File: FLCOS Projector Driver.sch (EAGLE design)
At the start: 61 parts, among them IC2 LM3414, IC3 MIC5219BM5, IC4 MIC5219BM5, IC5 LM3414, IC6 LM3414, Q1 14.31818MHz, Q3 12MHz, T2 S8050, T3 S8050, U1 TVP5150-NTSC_DECODER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

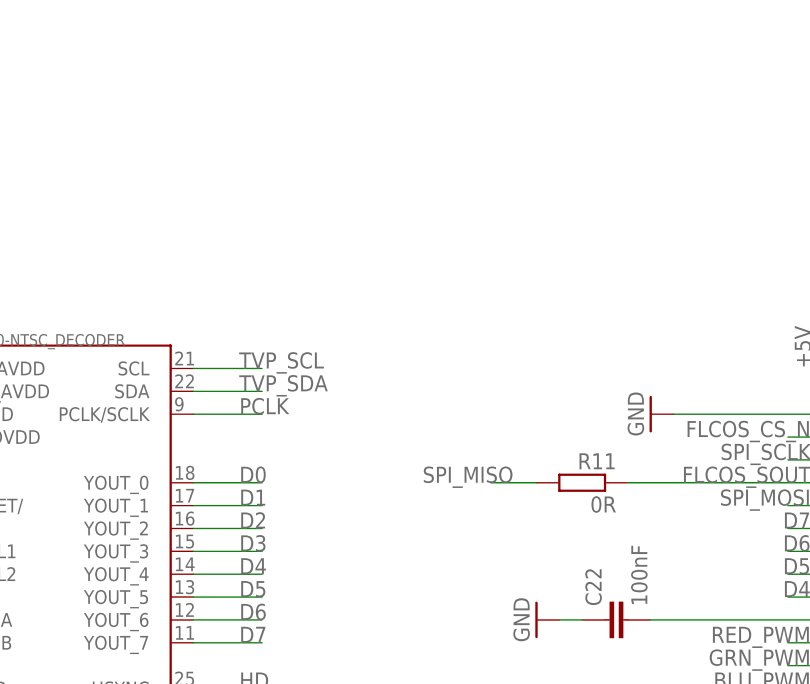
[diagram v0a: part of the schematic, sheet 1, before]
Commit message: added pullups to I2C
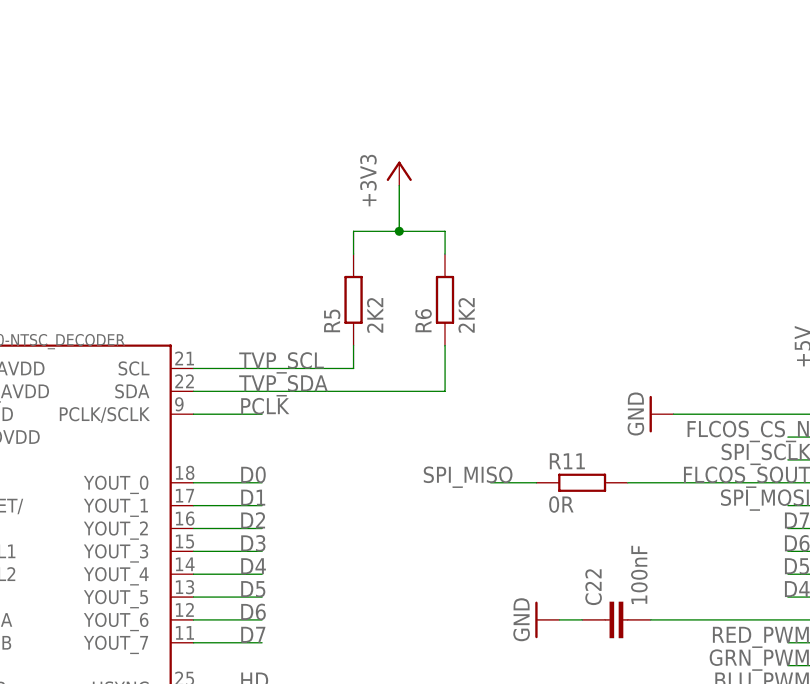
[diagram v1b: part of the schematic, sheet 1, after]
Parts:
- added R5, R6: 2K2, rcl:R-EU_R0603
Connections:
- net +3V3: now also R5.2, R6.2
- net FLCOS_SOUT: now also R11.2; no longer R11.1
- net SPI_MISO: now also R11.1; no longer R11.2
- net TVP_SCL: now also R5.1
- net TVP_SDA: now also R6.1
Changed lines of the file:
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@@
 <part name="P+8" library="supply1" deviceset="+5V" device=""/>
 <part name="P+9" library="supply1" deviceset="+5V" device=""/>
-<part name="R11" library="rcl" deviceset="R-EU_" device="R0603" value="0R"/>
 <part name="IC1" library="SparkFun" deviceset="V_REG_LM1117" device="SOT223"/>
 <part name="RGB" library="con-jst" deviceset="ZH-8" device=""/>
@@
 <part name="P+11" library="supply1" deviceset="+5V" device=""/>
 <part name="P+12" library="supply1" deviceset="+5V" device=""/>
+<part name="+3V3" library="supply1" deviceset="+3V3" device=""/>
+<part name="R11" library="rcl" deviceset="R-EU_" device="R0603" value="0R"/>
+<part name="R5" library="rcl" deviceset="R-EU_" device="R0603" value="2K2"/>
+<part name="R6" library="rcl" deviceset="R-EU_" device="R0603" value="2K2"/>
 </parts>
 <sheets>
@@
 <instance part="IC3" gate="G1" x="-40.64" y="71.12"/>
 <instance part="IC4" gate="G1" x="99.06" y="7.62"/>
-<instance part="R11" gate="G$1" x="109.22" y="63.5" rot="MR0"/>
 <instance part="IC1" gate="G$1" x="-38.1" y="106.68"/>
+<instance part="+3V3" gate="G$1" x="88.9" y="99.06"/>
+<instance part="R11" gate="G$1" x="109.22" y="63.5"/>
+<instance part="R5" gate="G$1" x="83.82" y="83.82" rot="R90"/>
+<instance part="R6" gate="G$1" x="93.98" y="83.82" rot="R90"/>
 </instances>
 <busses>
@@
 <segment>
 <pinref part="U1" gate="G$1" pin="SCL"/>
-<wire x1="66.04" y1="76.2" x2="73.66" y2="76.2" width="0.1524" layer="91"/>
 <label x="71.12" y="76.2" size="1.778" layer="95" rot="MR0" align="bottom-right"/>
+<wire x1="66.04" y1="76.2" x2="83.82" y2="76.2" width="0.1524" layer="91"/>
+<wire x1="83.82" y1="76.2" x2="83.82" y2="78.74" width="0.1524" layer="91"/>
+<pinref part="R5" gate="G$1" pin="1"/>
 </segment>
 </net>
@@
 <segment>
 <pinref part="U1" gate="G$1" pin="SDA"/>
-<wire x1="66.04" y1="73.66" x2="73.66" y2="73.66" width="0.1524" layer="91"/>
 <label x="71.12" y="73.66" size="1.778" layer="95" rot="MR0" align="bottom-right"/>
+<wire x1="66.04" y1="73.66" x2="93.98" y2="73.66" width="0.1524" layer="91"/>
+<wire x1="93.98" y1="73.66" x2="93.98" y2="78.74" width="0.1524" layer="91"/>
+<pinref part="R6" gate="G$1" pin="1"/>
 </segment>
 </net>
@@
 <pinref part="X1" gate="-5" pin="1"/>
 <label x="134.62" y="63.5" size="1.778" layer="95" rot="MR0"/>
-<pinref part="R11" gate="G$1" pin="1"/>
 <wire x1="139.7" y1="63.5" x2="114.3" y2="63.5" width="0.1524" layer="91"/>
+<pinref part="R11" gate="G$1" pin="2"/>
 </segment>
 </net>
@@
 <junction x="33.02" y="68.58"/>
 </segment>
+<segment>
+<wire x1="83.82" y1="88.9" x2="83.82" y2="91.44" width="0.1524" layer="91"/>
+<wire x1="83.82" y1="91.44" x2="88.9" y2="91.44" width="0.1524" layer="91"/>
+<wire x1="88.9" y1="91.44" x2="93.98" y2="91.44" width="0.1524" layer="91"/>
+<wire x1="93.98" y1="91.44" x2="93.98" y2="88.9" width="0.1524" layer="91"/>
+<pinref part="+3V3" gate="G$1" pin="+3V3"/>
+<wire x1="88.9" y1="91.44" x2="88.9" y2="96.52" width="0.1524" layer="91"/>
+<junction x="88.9" y="91.44"/>
+<pinref part="R5" gate="G$1" pin="2"/>
+<pinref part="R6" gate="G$1" pin="2"/>
+</segment>
 </net>
 <net name="EN_N" class="0">
@@
 <net name="SPI_MISO" class="0">
 <segment>
-<pinref part="R11" gate="G$1" pin="2"/>
 <wire x1="104.14" y1="63.5" x2="99.06" y2="63.5" width="0.1524" layer="91"/>
 <label x="101.6" y="63.5" size="1.778" layer="95" rot="MR0"/>
-</segment>
-</net>
+<pinref part="R11" gate="G$1" pin="1"/>
+</segment>
+</net>

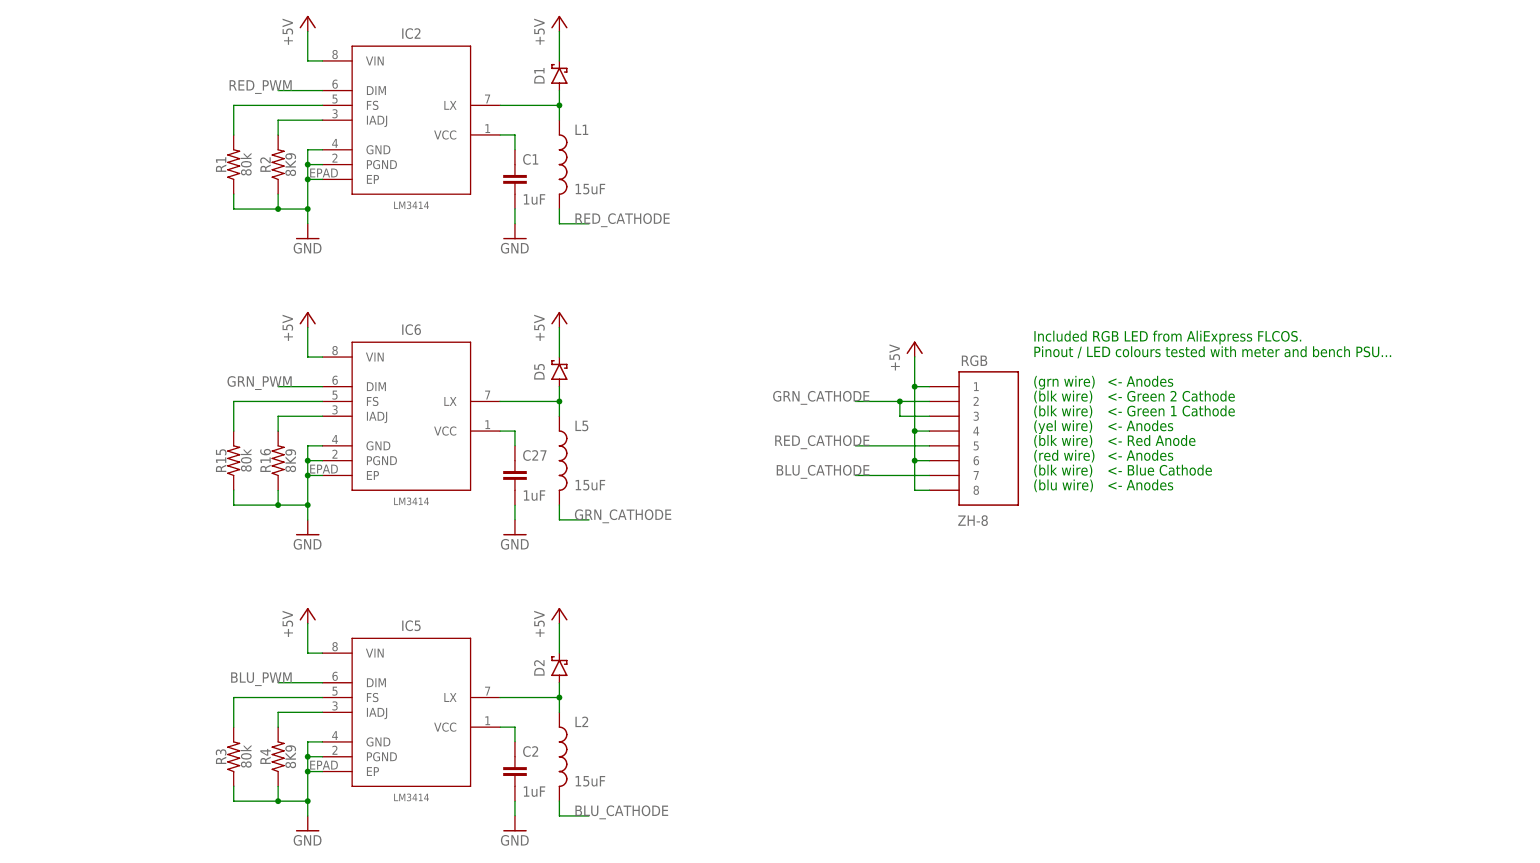
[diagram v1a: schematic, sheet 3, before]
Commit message: RGB LED current set to 156mA
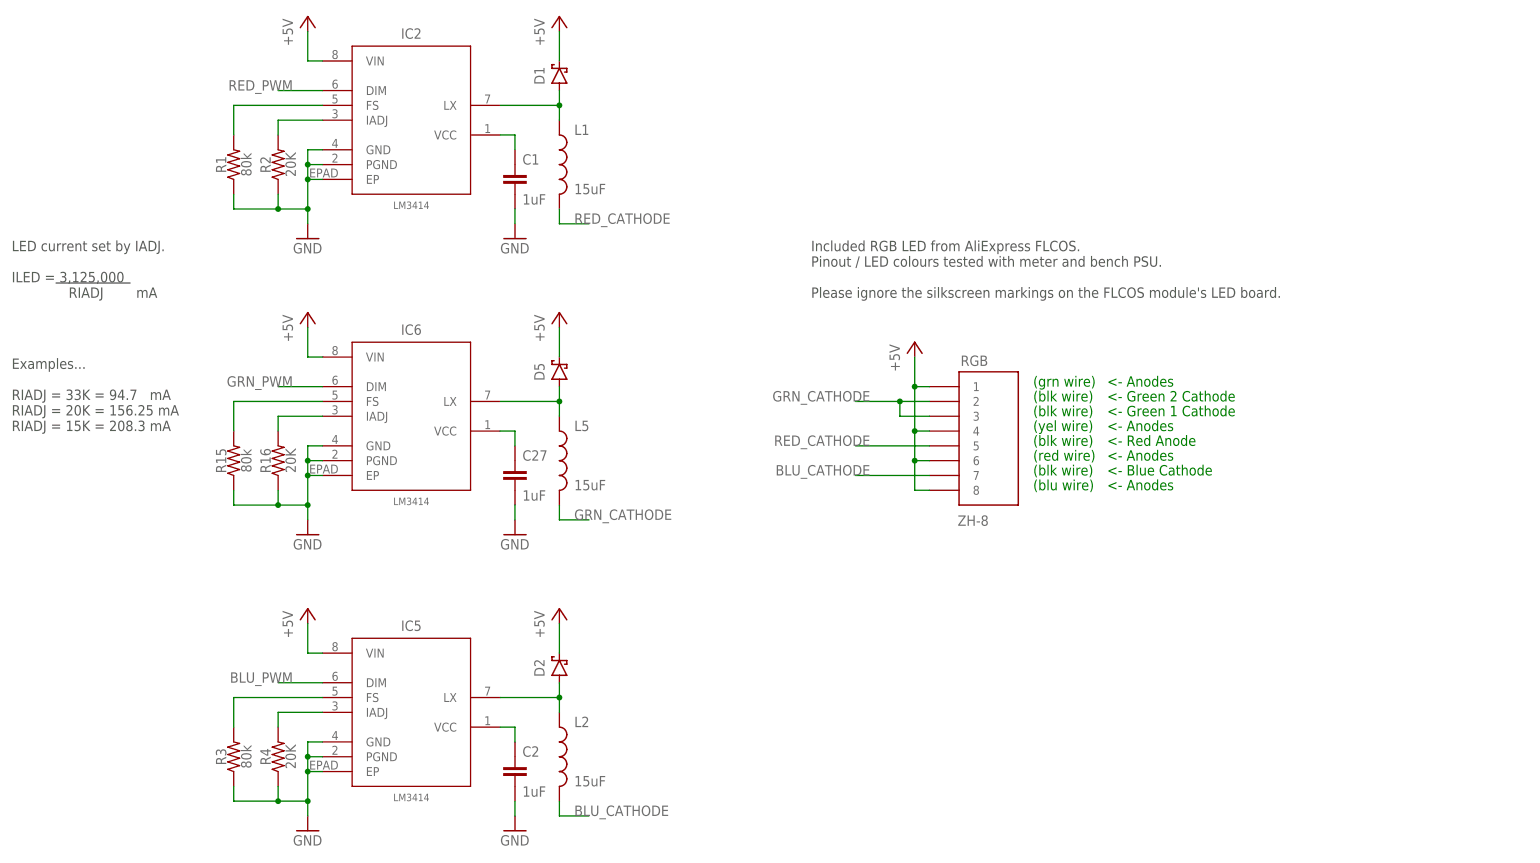
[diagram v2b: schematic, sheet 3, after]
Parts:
- R16, R2, R4: value 8K9 -> 20K
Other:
- note added: "Examples... RIADJ = 33K = 94.7 mA RIADJ = 20K = 156.25 mA RIADJ = 15K = 208.3 mA"
- note added: "Included RGB LED from AliExpress FLCOS. Pinout / LED colours tested with meter and bench PSU. Please ignore the silkscreen markings on the FLCOS module's LED board."
- note added: "LED current set by IADJ. ILED = 3,125,000 RIADJ mA"
- note removed: "Included RGB LED from AliExpress FLCOS. Pinout / LED colours tested with meter and bench PSU..."
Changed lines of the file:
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@@
 <part name="C27" library="A_butts" deviceset="CAPACITOR-CERAMIC" device="C0603" value="1uF"/>
 <part name="R15" library="A_butts" deviceset="RESISTOR" device="R0603" value="80k"/>
-<part name="R16" library="A_butts" deviceset="RESISTOR" device="R0603" value="8K9"/>
+<part name="R16" library="A_butts" deviceset="RESISTOR" device="R0603" value="20K"/>
 <part name="IC6" library="A_butts" deviceset="LM3414" device="SO08-PAD" value="LM3414"/>
 <part name="GND33" library="A_butts" deviceset="GND" device=""/>
@@
 <part name="C1" library="A_butts" deviceset="CAPACITOR-CERAMIC" device="C0603" value="1uF"/>
 <part name="R1" library="A_butts" deviceset="RESISTOR" device="R0603" value="80k"/>
-<part name="R2" library="A_butts" deviceset="RESISTOR" device="R0603" value="8K9"/>
+<part name="R2" library="A_butts" deviceset="RESISTOR" device="R0603" value="20K"/>
 <part name="IC2" library="A_butts" deviceset="LM3414" device="SO08-PAD" value="LM3414"/>
 <part name="GND4" library="A_butts" deviceset="GND" device=""/>
@@
 <part name="C2" library="A_butts" deviceset="CAPACITOR-CERAMIC" device="C0603" value="1uF"/>
 <part name="R3" library="A_butts" deviceset="RESISTOR" device="R0603" value="80k"/>
-<part name="R4" library="A_butts" deviceset="RESISTOR" device="R0603" value="8K9"/>
+<part name="R4" library="A_butts" deviceset="RESISTOR" device="R0603" value="20K"/>
 <part name="IC5" library="A_butts" deviceset="LM3414" device="SO08-PAD" value="LM3414"/>
 <part name="GND6" library="A_butts" deviceset="GND" device=""/>
@@
 <text x="170.18" y="73.66" size="1.778" layer="91">&lt;- Anodes</text>
 <text x="170.18" y="60.96" size="1.778" layer="91">&lt;- Anodes</text>
-<text x="157.48" y="78.74" size="1.778" layer="91">Included RGB LED from AliExpress FLCOS.
-Pinout / LED colours tested with meter and bench PSU...</text>
+<text x="119.38" y="88.9" size="1.778" layer="97">Included RGB LED from AliExpress FLCOS.
+Pinout / LED colours tested with meter and bench PSU.
+Please ignore the silkscreen markings on the FLCOS module's LED board.</text>
+<text x="-17.78" y="88.9" size="1.778" layer="97">LED current set by IADJ.
+ILED = 3,125,000
+              RIADJ        mA</text>
+<wire x1="-10.16" y1="91.44" x2="2.54" y2="91.44" width="0.1524" layer="97"/>
+<text x="-17.78" y="66.04" size="1.778" layer="97">Examples...
+RIADJ = 33K = 94.7   mA
+RIADJ = 20K = 156.25 mA
+RIADJ = 15K = 208.3 mA</text>
 </plain>
 <instances>

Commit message: schematic tweaks
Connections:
- net D0 renamed FLCOS_D0
- net D1 renamed FLCOS_D1
- net D2 renamed FLCOS_D2
- net D3 renamed FLCOS_D3
- net D4 renamed FLCOS_D4
- net D5 renamed FLCOS_D5
- net D6 renamed FLCOS_D6
- net D7 renamed FLCOS_D7
- net HD renamed FLCOS_HD
- net PCLK renamed FLCOS_PCLK
- net VALID renamed FLCOS_VALID
- net VD renamed FLCOS_VD
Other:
- moved on the sheet: C20, C21, C23, JP2, R10, R7, R8, R9

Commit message: Allow USB/GPIO0 to reset TVP and FLCOS
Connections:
- removed net EN_N: R67.1, T3.C, U1.RESET/, U2.EN, X1-23.1
- removed net GPIO0: T2.C, U2.IO0
- new net ESP_EN_N: R67.1, T3.C, U2.EN
- new net TVP_FL_RST_N: T2.C, U1.RESET/, U2.IO0, X1-23.1
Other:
- note added: "GPIO0! ->"
- moved on the sheet: C14, C15, Q1, R67
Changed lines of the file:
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@@
 <instance part="U1" gate="G$1" x="50.8" y="53.34"/>
 <instance part="GND19" gate="1" x="33.02" y="17.78"/>
-<instance part="GND20" gate="1" x="-10.16" y="60.96" rot="R270"/>
-<instance part="GND21" gate="1" x="-10.16" y="50.8" rot="R270"/>
-<instance part="C14" gate="G$1" x="-2.54" y="60.96" rot="R90"/>
-<instance part="C15" gate="G$1" x="-2.54" y="50.8" rot="R90"/>
+<instance part="GND20" gate="1" x="-10.16" y="58.42" rot="R270"/>
+<instance part="GND21" gate="1" x="-10.16" y="48.26" rot="R270"/>
+<instance part="C14" gate="G$1" x="-2.54" y="58.42" rot="R90"/>
+<instance part="C15" gate="G$1" x="-2.54" y="48.26" rot="R90"/>
 <instance part="C16" gate="G$1" x="0" y="30.48" rot="R180"/>
 <instance part="C17" gate="G$1" x="20.32" y="30.48" rot="R180"/>
@@
 <instance part="GND24" gate="1" x="-20.32" y="2.54" rot="R90"/>
 <instance part="GND25" gate="1" x="-20.32" y="30.48" rot="R90"/>
-<instance part="Q1" gate="G$1" x="7.62" y="55.88" rot="R90"/>
+<instance part="Q1" gate="G$1" x="7.62" y="53.34" rot="R90"/>
 <instance part="JP2" gate="A" x="-71.12" y="22.86" rot="MR0"/>
 <instance part="GND26" gate="1" x="-63.5" y="15.24"/>
@@
 <pinref part="GND21" gate="1" pin="GND"/>
 <pinref part="C15" gate="G$1" pin="1"/>
-<wire x1="-7.62" y1="50.8" x2="-5.08" y2="50.8" width="0.1524" layer="91"/>
+<wire x1="-7.62" y1="48.26" x2="-5.08" y2="48.26" width="0.1524" layer="91"/>
 </segment>
 <segment>
 <pinref part="GND20" gate="1" pin="GND"/>
 <pinref part="C14" gate="G$1" pin="1"/>
-<wire x1="-7.62" y1="60.96" x2="-5.08" y2="60.96" width="0.1524" layer="91"/>
+<wire x1="-7.62" y1="58.42" x2="-5.08" y2="58.42" width="0.1524" layer="91"/>
 </segment>
 <segment>
@@
 <pinref part="U1" gate="G$1" pin="XTAL1"/>
 <label x="30.48" y="55.88" size="1.778" layer="95" rot="MR0"/>
-<wire x1="7.62" y1="58.42" x2="7.62" y2="60.96" width="0.1524" layer="91"/>
-<wire x1="7.62" y1="60.96" x2="15.24" y2="60.96" width="0.1524" layer="91"/>
-<wire x1="15.24" y1="60.96" x2="15.24" y2="55.88" width="0.1524" layer="91"/>
+<wire x1="7.62" y1="55.88" x2="7.62" y2="58.42" width="0.1524" layer="91"/>
+<wire x1="7.62" y1="58.42" x2="15.24" y2="58.42" width="0.1524" layer="91"/>
+<wire x1="15.24" y1="58.42" x2="15.24" y2="55.88" width="0.1524" layer="91"/>
 <wire x1="15.24" y1="55.88" x2="35.56" y2="55.88" width="0.1524" layer="91"/>
 <pinref part="C14" gate="G$1" pin="2"/>
-<wire x1="2.54" y1="60.96" x2="7.62" y2="60.96" width="0.1524" layer="91"/>
-<junction x="7.62" y="60.96"/>
+<wire x1="2.54" y1="58.42" x2="7.62" y2="58.42" width="0.1524" layer="91"/>
+<junction x="7.62" y="58.42"/>
 <pinref part="Q1" gate="G$1" pin="2"/>
 </segment>
@@
 <label x="30.48" y="53.34" size="1.778" layer="95" rot="MR0"/>
 <wire x1="35.56" y1="53.34" x2="15.24" y2="53.34" width="0.1524" layer="91"/>
-<wire x1="15.24" y1="53.34" x2="15.24" y2="50.8" width="0.1524" layer="91"/>
-<wire x1="15.24" y1="50.8" x2="7.62" y2="50.8" width="0.1524" layer="91"/>
-<wire x1="7.62" y1="50.8" x2="7.62" y2="53.34" width="0.1524" layer="91"/>
+<wire x1="15.24" y1="53.34" x2="15.24" y2="48.26" width="0.1524" layer="91"/>
+<wire x1="15.24" y1="48.26" x2="7.62" y2="48.26" width="0.1524" layer="91"/>
+<wire x1="7.62" y1="48.26" x2="7.62" y2="50.8" width="0.1524" layer="91"/>
 <pinref part="C15" gate="G$1" pin="2"/>
-<wire x1="2.54" y1="50.8" x2="7.62" y2="50.8" width="0.1524" layer="91"/>
-<junction x="7.62" y="50.8"/>
+<wire x1="2.54" y1="48.26" x2="7.62" y2="48.26" width="0.1524" layer="91"/>
+<junction x="7.62" y="48.26"/>
 <pinref part="Q1" gate="G$1" pin="1"/>
 </segment>
@@
 </segment>
 </net>
-<net name="EN_N" class="0">
+<net name="TVP_FL_RST_N" class="0">
 <segment>
 <pinref part="U1" gate="G$1" pin="RESET/"/>
@@
 get crossed over here!
 (null-modem style)</text>
+<text x="-5.08" y="104.14" size="1.778" layer="97">GPIO0! -&gt;</text>
 </plain>
 <instances>
@@
 <instance part="GND67" gate="1" x="55.88" y="66.04" rot="R270"/>
 <instance part="GND68" gate="1" x="73.66" y="7.62"/>
-<instance part="R67" gate="G$1" x="45.72" y="66.04" rot="MR90"/>
-<instance part="U$12" gate="G$1" x="45.72" y="76.2"/>
+<instance part="R67" gate="G$1" x="43.18" y="66.04" rot="MR90"/>
+<instance part="U$12" gate="G$1" x="43.18" y="76.2"/>
 <instance part="U$10" gate="G$1" x="195.58" y="45.72"/>
 <instance part="GND53" gate="1" x="172.72" y="20.32" smashed="yes">
@@
 <pinref part="R67" gate="G$1" pin="2"/>
 <pinref part="U$12" gate="G$1" pin="+3V3"/>
-<wire x1="45.72" y1="71.12" x2="45.72" y2="73.66" width="0.1524" layer="91"/>
+<wire x1="43.18" y1="71.12" x2="43.18" y2="73.66" width="0.1524" layer="91"/>
 </segment>
 <segment>
@@
 </segment>
 </net>
-<net name="EN_N" class="0">
+<net name="ESP_EN_N" class="0">
 <segment>
 <pinref part="U2" gate="G$1" pin="EN"/>
 <pinref part="R67" gate="G$1" pin="1"/>
-<wire x1="63.5" y1="55.88" x2="45.72" y2="55.88" width="0.1524" layer="91"/>
-<wire x1="45.72" y1="55.88" x2="45.72" y2="60.96" width="0.1524" layer="91"/>
+<wire x1="63.5" y1="55.88" x2="43.18" y2="55.88" width="0.1524" layer="91"/>
+<wire x1="43.18" y1="55.88" x2="43.18" y2="60.96" width="0.1524" layer="91"/>
 <label x="58.42" y="55.88" size="1.778" layer="95" rot="MR0"/>
 </segment>
@@
 </segment>
 </net>
-<net name="GPIO0" class="0">
+<net name="TVP_FL_RST_N" class="0">
 <segment>
 <pinref part="T2" gate="G$1" pin="C"/>
